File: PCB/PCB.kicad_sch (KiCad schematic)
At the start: 20 parts, among them U1 STM32G031F6P6, U2 A7106, U3 HT7333-3.3V, Y1 16MHz

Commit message: Organise the schematic
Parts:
- removed CH1: Channel 1, TestPoint:TestPoint_THTPad_1.0x1.0mm_Drill0.5mm, symbol Connector:TestPoint
- removed CH2: Channel 2, TestPoint:TestPoint_THTPad_1.0x1.0mm_Drill0.5mm, symbol Connector:TestPoint
- removed CH3: Channel 3, TestPoint:TestPoint_THTPad_1.0x1.0mm_Drill0.5mm, symbol Connector:TestPoint
- removed GND1: Ground, TestPoint:TestPoint_THTPad_1.0x1.0mm_Drill0.5mm, symbol Connector:TestPoint
- removed VCC1: Power, TestPoint:TestPoint_THTPad_1.0x1.0mm_Drill0.5mm, symbol Connector:TestPoint
- added C5: 100nF, Capacitor_SMD:C_0402_1005Metric, symbol Device:C
- added C8: 1µF, symbol Device:C
- added J1: Conn_01x06_Pin, Connector_PinHeader_2.54mm:PinHeader_1x06_P2.54mm_Vertical, symbol Connector:Conn_01x06_Pin
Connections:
- net GND: now reaches C2.2, C3.2, C6.1, U1.20 (VSS), U2.15 (GND), U3.2 (GND), Y1.1
- net GND: now also C5.1, C8.1, J1.1 (Pin_1); no longer U2.7 (GND)
- net at C6.2: no longer U2.2 (BPBG)
- net at C7.1: now also J1.2 (Pin_2)
- net at U2.1 (RSSI): now also ANT1.2 (PCB_Trace)
- net +3.3V: now reaches C4.1, R1.2, U2.20 (VDA1), U2.5 (VDA2), U3.3 (VOUT)
- net +3.3V: now also U2.8 (XI); no longer U2.10 (VDA3)
- net at U2.13 (DVDD): now also C5.2
- net GIO2: now reaches U1.16 (PB0), U2.17 (GIO2)
- net at U2.19 (REGI): now also C8.2
- net at U2.3 (RFI): no longer ANT1.2 (PCB_Trace)
- net at L1.1: now also U2.2 (BPBG); no longer U2.4 (RFO)
- net at U2.6 (VT): now also C2.1
- net at C3.1, Y1.2: now also U2.7 (GND); no longer U2.9 (XO)
- new net CH1: J1.3 (Pin_3)
- new net CH2: J1.4 (Pin_4)
- new net CH3: J1.5 (Pin_5)
- new net CH4: J1.6 (Pin_6)
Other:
- moved on the sheet: ANT1, C1, C2, C3, C4, C6, C7, L1, R1, TP1, TP2, U1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

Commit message: More schematic updates
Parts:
- removed C4: 100nF, Capacitor_SMD:C_0402_1005Metric, symbol Device:C
- removed R1: 10k, Resistor_SMD:R_0402_1005Metric, symbol Device:R
- removed TP1: SWDIO, TestPoint:TestPoint_Pad_D1.0mm, symbol Connector:TestPoint
- removed TP2: SWCLK, TestPoint:TestPoint_Pad_D1.0mm, symbol Connector:TestPoint
- removed U1: STM32G031F6P6, Package_SO:TSSOP-20_4.4x6.5mm_P0.65mm, symbol Nano2A:STM32G031F6P6
- added C9: 100nF, Capacitor_SMD:C_0402_1005Metric, symbol Device:C
- added TP3: SWDIO, TestPoint:TestPoint_Pad_D1.0mm, symbol Connector:TestPoint
- added TP4: SWCLK, TestPoint:TestPoint_Pad_D1.0mm, symbol Connector:TestPoint
- added U4: STM32G031F6Px, Package_SO:TSSOP-20_4.4x6.5mm_P0.65mm, symbol MCU_ST_STM32G0:STM32G031F6Px
- C2, C3: value 22pF -> 18pF
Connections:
- net +3.3V: now also C9.1; no longer U2.8 (XI)
- net GIO1: now also U4.14 (PA7)
- net GIO2: now also U4.15 (PA8/PB0/PB1/PB2)
- net GND: now also C2.1, U2.7 (GND), U4.5 (VSS); no longer C2.2, Y1.1
- net SCK: now also U4.12 (PA5)
- net SCS: now also U4.10 (PA3)
- net SDIO: now also U4.13 (PA6)
- net at C6.2: now also U2.1 (RSSI)
- net at ANT1.2 (PCB_Trace): now also U2.3 (RFI); no longer U2.1 (RSSI)
- net at U2.2 (BPBG): no longer L1.1
- net at U2.4 (RFO): now also L1.1
- net at U2.6 (VT): no longer C2.1
- net at C3.1, Y1.2: now also U2.9 (XO); no longer U2.7 (GND)
- new net: TP3.1, U4.18 (PA13)
- new net: TP4.1, U4.19 (PA14/PA15)
- new net: C9.2, U4.4 (VDD)
- new net: C2.2, U2.8 (XI), Y1.1
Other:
- note added: "Input & Power"
- note added: "Microcontroller"
- note added: "Transceiver"
- moved on the sheet: ANT1, C1, C2, C3, C6, L1, Y1

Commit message: Wiring fixes
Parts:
- added C10: 1.5nF, Capacitor_SMD:C_0402_1005Metric, symbol Device:C
- added C11: 100nF, Capacitor_SMD:C_0402_1005Metric, symbol Device:C
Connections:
- net +3.3V: now also C5.2, C8.2, U2.10 (VDA3), U2.13 (DVDD), U2.19 (REGI)
- net CH1: now also U4.10 (PA3)
- net CH2: now also U4.9 (PA2)
- net CH3: now also U4.8 (PA1)
- net CH4: now also U4.7 (PA0)
- net GND: now also C10.2, C11.2
- net SCS: now also U4.11 (PA4); no longer U4.10 (PA3)
- net at U2.2 (BPBG): now also C10.1
- net at U2.6 (VT): now also C11.1
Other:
- moved on the sheet: C2, C3, C5, C6, C7, C8, C9, J1, TP3, TP4, U3, U4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

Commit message: Final PCB fixes
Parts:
- added C12, C13, C14: 100nF, Capacitor_SMD:C_0402_1005Metric, symbol Device:C
- added R1: 10k, symbol Device:R
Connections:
- net +3.3V: now also U4.4 (VDD), R1.1; no longer U2.10 (VDA3), U2.20 (VDA1), U2.5 (VDA2)
- net CH1: now also J1.6 (Pin_6); no longer J1.3 (Pin_3)
- net CH2: now also J1.5 (Pin_5); no longer J1.4 (Pin_4)
- net CH3: now also J1.4 (Pin_4); no longer J1.5 (Pin_5)
- net CH4: now also J1.3 (Pin_3); no longer J1.6 (Pin_6)
- net GND: now also C7.1, C9.2, C12.1, C13.1, C14.1
- net at U4.6 (PF2): now also R1.2
- net at J1.2 (Pin_2): now also C7.2, U3.1 (VIN); no longer C7.1
- new net VDA3: C12.2, C13.2, C14.2, U2.10 (VDA3), U2.20 (VDA1), U2.5 (VDA2)
- no-connect marks 0 -> 7
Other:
- note added: "CH1"
- note added: "CH2"
- note added: "CH3"
- note added: "CH4"
- note added: "GND"
- note added: "VCC"
- moved on the sheet: C7, C9, J1, U3

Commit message: Add footprints to components
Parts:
- C8: footprint (none) -> Capacitor_SMD:C_0402_1005Metric
- R1: footprint (none) -> Resistor_SMD:R_0402_1005Metric
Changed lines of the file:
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@@
 			)
 		)
-		(property "Footprint" ""
+		(property "Footprint" "Capacitor_SMD:C_0402_1005Metric"
 			(at 209.2452 54.61 0)
 			(hide yes)
@@
 			)
 		)
-		(property "Footprint" ""
+		(property "Footprint" "Resistor_SMD:R_0402_1005Metric"
 			(at 92.71 70.358 90)
 			(hide yes)

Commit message: Antenna fixes
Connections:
- net GND: now also ANT1.2 (PCB_Trace), U2.21 (EP)
- net at U2.3 (RFI): now also L1.1, U2.4 (RFO); no longer ANT1.2 (PCB_Trace)
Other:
- moved on the sheet: ANT1, C1, C13, L1

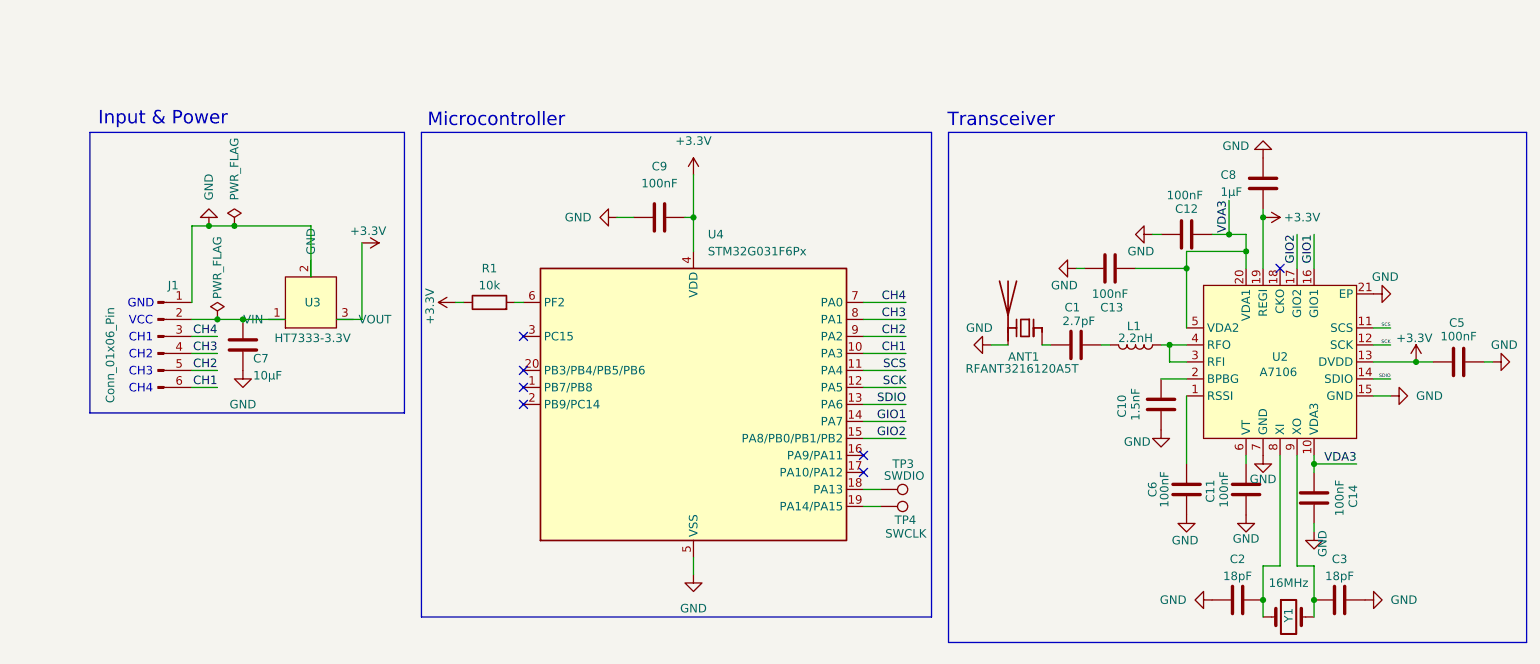
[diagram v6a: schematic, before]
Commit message: Better antenna matching
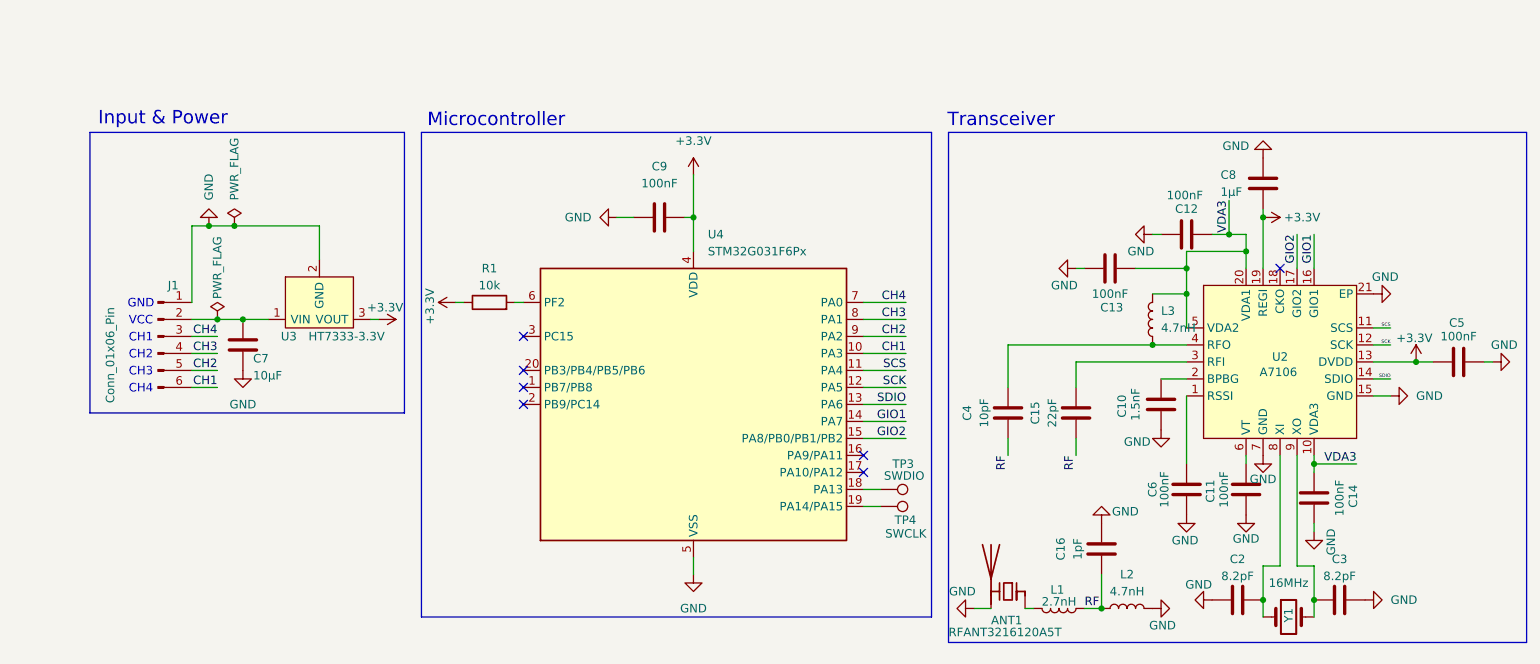
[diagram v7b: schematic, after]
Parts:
- removed C1: 2.7pF, Capacitor_SMD:C_0402_1005Metric, symbol Device:C
- added C15: 22pF, Capacitor_SMD:C_0402_1005Metric, symbol Device:C
- added C16: 1pF, Capacitor_SMD:C_0402_1005Metric, symbol Device:C
- added C4: 10pF, Capacitor_SMD:C_0402_1005Metric, symbol Device:C
- added L2, L3: 4.7nH, symbol Device:L
- C2, C3: value 18pF -> 8.2pF
- L1: value 2.2nH -> 2.7nH
- Y1: LCSC C12668 -> C13738
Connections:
- net GND: now also C16.2, L2.2
- net VDA3: now also L3.2
- net at L1.2: now also ANT1.1 (FEED)
- new net: C15.2, U2.3 (RFI)
- new net: C4.2, L3.1, U2.4 (RFO)
- new net RF: C15.1, C16.1, C4.1, L1.1, L2.1
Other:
- moved on the sheet: ANT1, L1, U3

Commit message: Add battery voltage reader
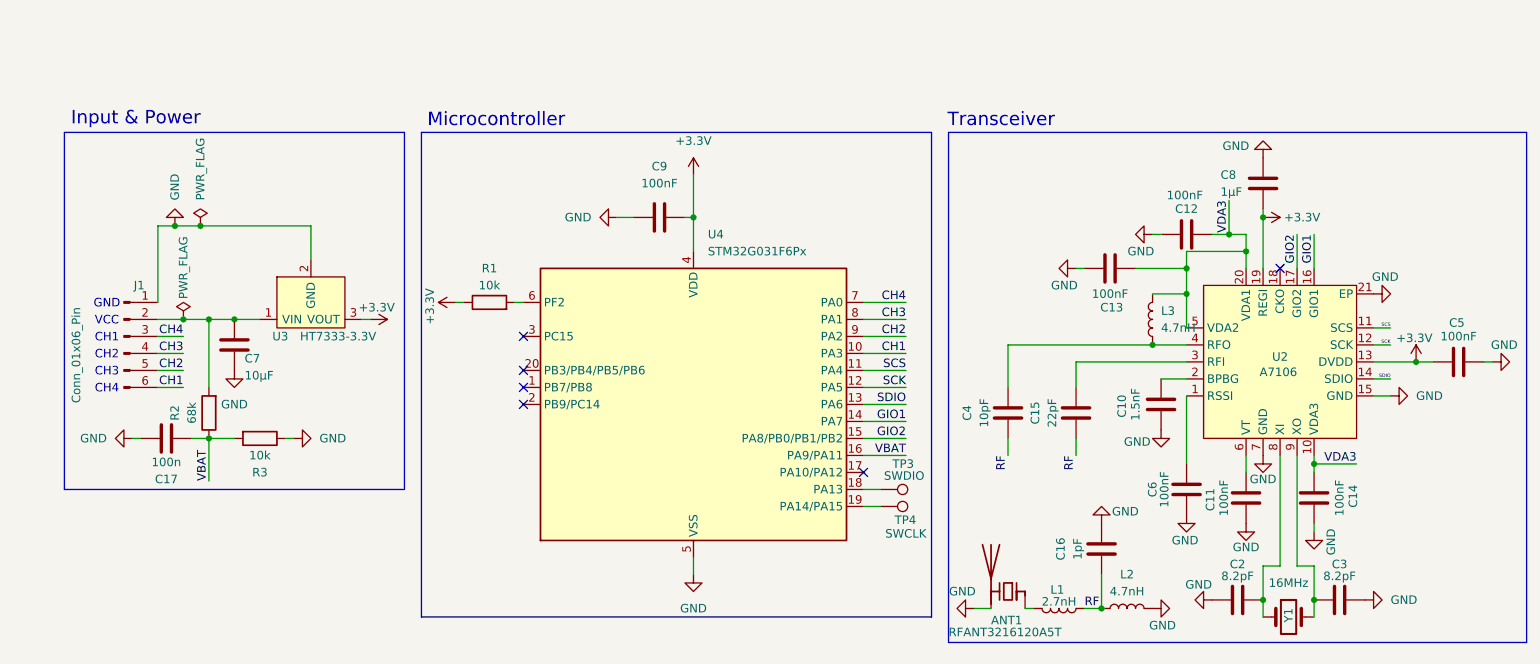
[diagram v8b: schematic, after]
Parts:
- added C17: 100n, Capacitor_SMD:C_0402_1005Metric, symbol Device:C
- added R2: 68k, Resistor_SMD:R_0402_1005Metric, symbol Device:R
- added R3: 10k, Resistor_SMD:R_0402_1005Metric, symbol Device:R
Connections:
- net GND: now also C17.2, R3.1
- net VBAT: now reaches U4.16 (PA9/PA11)
- net VBAT: now also C17.1, R2.1, R3.2
- net at C7.2, J1.2 (Pin_2), U3.1 (VIN): now also R2.2
- no-connect marks 7 -> 6
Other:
- moved on the sheet: C11, C7, J1, U3
